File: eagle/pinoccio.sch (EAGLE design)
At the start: 60 parts, among them IC1 ATMEGA16U2QFN32, J1 AVR_SPI_PRG_6, Q1 16MHz, Q2 32.768k, Q3 16MHz, U1 MCP73831, U2 TPS78233, U4 ATMEGA128RFA1, X1 USB-MICROB, Y2 ANTENNA2SMD5

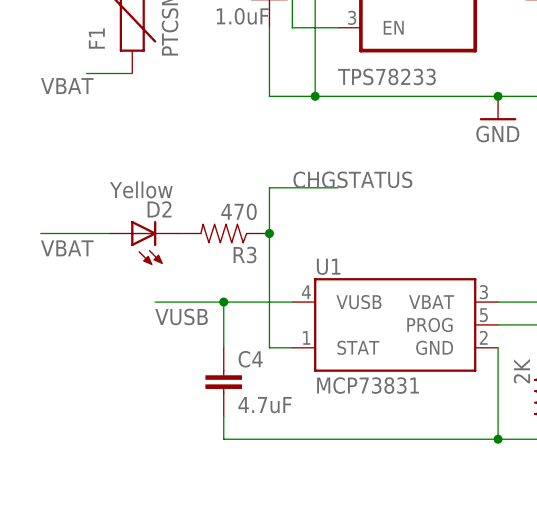
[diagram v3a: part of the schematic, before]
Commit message: Adjust a couple of spacing issues
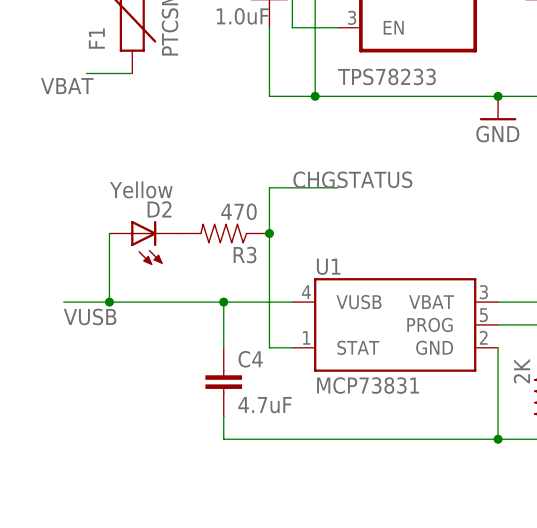
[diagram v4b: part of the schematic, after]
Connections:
- net VBAT: no longer D2.A
- net VUSB: now also D2.A
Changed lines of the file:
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@@
 <segment>
 <wire x1="25.4" y1="17.78" x2="25.4" y2="22.86" width="0.1524" layer="91"/>
-<label x="17.78" y="20.32" size="1.778" layer="95"/>
+<label x="7.62" y="20.32" size="1.778" layer="95"/>
 <pinref part="C4" gate="G$1" pin="1"/>
-<wire x1="25.4" y1="22.86" x2="17.78" y2="22.86" width="0.1524" layer="91"/>
+<wire x1="25.4" y1="22.86" x2="12.7" y2="22.86" width="0.1524" layer="91"/>
 <pinref part="U1" gate="G$1" pin="VUSB"/>
+<wire x1="12.7" y1="22.86" x2="7.62" y2="22.86" width="0.1524" layer="91"/>
 <wire x1="25.4" y1="22.86" x2="33.02" y2="22.86" width="0.1524" layer="91"/>
 <junction x="25.4" y="22.86"/>
+<pinref part="D2" gate="G$1" pin="A"/>
+<wire x1="12.7" y1="30.48" x2="12.7" y2="22.86" width="0.1524" layer="91"/>
+<junction x="12.7" y="22.86"/>
 </segment>
 <segment>
@@
 <label x="137.16" y="12.7" size="1.778" layer="95"/>
 </segment>
-<segment>
-<pinref part="D2" gate="G$1" pin="A"/>
-<wire x1="12.7" y1="30.48" x2="5.08" y2="30.48" width="0.1524" layer="91"/>
-<label x="5.08" y="27.94" size="1.778" layer="95"/>
-</segment>
 </net>

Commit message: Tagging for v0.9
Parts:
- R1: value 10k -> 2k
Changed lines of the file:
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@@
 <grid distance="0.1" unitdist="inch" unit="inch" style="lines" multiple="1" display="no" altdistance="0.01" altunitdist="inch" altunit="inch"/>
 <layers>
-<layer number="1" name="Top" color="4" fill="1" visible="no" active="no"/>
-<layer number="2" name="Route2" color="1" fill="3" visible="no" active="no"/>
-<layer number="3" name="Route3" color="4" fill="3" visible="no" active="no"/>
-<layer number="4" name="Route4" color="1" fill="4" visible="no" active="no"/>
-<layer number="5" name="Route5" color="4" fill="4" visible="no" active="no"/>
-<layer number="6" name="Route6" color="1" fill="8" visible="no" active="no"/>
-<layer number="7" name="Route7" color="4" fill="8" visible="no" active="no"/>
-<layer number="8" name="Route8" color="1" fill="2" visible="no" active="no"/>
-<layer number="9" name="Route9" color="4" fill="2" visible="no" active="no"/>
-<layer number="10" name="Route10" color="1" fill="7" visible="no" active="no"/>
-<layer number="11" name="Route11" color="4" fill="7" visible="no" active="no"/>
-<layer number="12" name="Route12" color="1" fill="5" visible="no" active="no"/>
-<layer number="13" name="Route13" color="4" fill="5" visible="no" active="no"/>
-<layer number="14" name="Route14" color="1" fill="6" visible="no" active="no"/>
-<layer number="15" name="Route15" color="4" fill="6" visible="no" active="no"/>
-<layer number="16" name="Bottom" color="1" fill="1" visible="no" active="no"/>
-<layer number="17" name="Pads" color="2" fill="1" visible="no" active="no"/>
-<layer number="18" name="Vias" color="2" fill="1" visible="no" active="no"/>
-<layer number="19" name="Unrouted" color="6" fill="1" visible="no" active="no"/>
-<layer number="20" name="Dimension" color="6" fill="1" visible="no" active="no"/>
-<layer number="21" name="tPlace" color="16" fill="1" visible="no" active="no"/>
-<layer number="22" name="bPlace" color="14" fill="1" visible="no" active="no"/>
-<layer number="23" name="tOrigins" color="15" fill="1" visible="no" active="no"/>
-<layer number="24" name="bOrigins" color="15" fill="1" visible="no" active="no"/>
-<layer number="25" name="tNames" color="7" fill="1" visible="no" active="no"/>
-<layer number="26" name="bNames" color="7" fill="1" visible="no" active="no"/>
-<layer number="27" name="tValues" color="7" fill="1" visible="no" active="no"/>
-<layer number="28" name="bValues" color="7" fill="1" visible="no" active="no"/>
+<layer number="1" name="Top" color="4" fill="1" visible="yes" active="no"/>
+<layer number="2" name="Route2" color="1" fill="3" visible="yes" active="no"/>
+<layer number="3" name="Route3" color="4" fill="3" visible="yes" active="no"/>
+<layer number="4" name="Route4" color="1" fill="4" visible="yes" active="no"/>
+<layer number="5" name="Route5" color="4" fill="4" visible="yes" active="no"/>
+<layer number="6" name="Route6" color="1" fill="8" visible="yes" active="no"/>
+<layer number="7" name="Route7" color="4" fill="8" visible="yes" active="no"/>
+<layer number="8" name="Route8" color="1" fill="2" visible="yes" active="no"/>
+<layer number="9" name="Route9" color="4" fill="2" visible="yes" active="no"/>
+<layer number="10" name="Route10" color="1" fill="7" visible="yes" active="no"/>
+<layer number="11" name="Route11" color="4" fill="7" visible="yes" active="no"/>
+<layer number="12" name="Route12" color="1" fill="5" visible="yes" active="no"/>
+<layer number="13" name="Route13" color="4" fill="5" visible="yes" active="no"/>
+<layer number="14" name="Route14" color="1" fill="6" visible="yes" active="no"/>
+<layer number="15" name="Route15" color="4" fill="6" visible="yes" active="no"/>
+<layer number="16" name="Bottom" color="1" fill="1" visible="yes" active="no"/>
+<layer number="17" name="Pads" color="2" fill="1" visible="yes" active="no"/>
+<layer number="18" name="Vias" color="2" fill="1" visible="yes" active="no"/>
+<layer number="19" name="Unrouted" color="6" fill="1" visible="yes" active="no"/>
+<layer number="20" name="Dimension" color="6" fill="1" visible="yes" active="no"/>
+<layer number="21" name="tPlace" color="16" fill="1" visible="yes" active="no"/>
+<layer number="22" name="bPlace" color="14" fill="1" visible="yes" active="no"/>
+<layer number="23" name="tOrigins" color="15" fill="1" visible="yes" active="no"/>
+<layer number="24" name="bOrigins" color="15" fill="1" visible="yes" active="no"/>
+<layer number="25" name="tNames" color="7" fill="1" visible="yes" active="no"/>
+<layer number="26" name="bNames" color="7" fill="1" visible="yes" active="no"/>
+<layer number="27" name="tValues" color="7" fill="1" visible="yes" active="no"/>
+<layer number="28" name="bValues" color="7" fill="1" visible="yes" active="no"/>
 <layer number="29" name="tStop" color="5" fill="1" visible="no" active="no"/>
 <layer number="30" name="bStop" color="7" fill="6" visible="no" active="no"/>
@@
 <layer number="35" name="tGlue" color="7" fill="4" visible="no" active="no"/>
 <layer number="36" name="bGlue" color="7" fill="5" visible="no" active="no"/>
-<layer number="37" name="tTest" color="7" fill="1" visible="no" active="no"/>
-<layer number="38" name="bTest" color="7" fill="1" visible="no" active="no"/>
+<layer number="37" name="tTest" color="7" fill="1" visible="yes" active="no"/>
+<layer number="38" name="bTest" color="7" fill="1" visible="yes" active="no"/>
 <layer number="39" name="tKeepout" color="4" fill="11" visible="no" active="no"/>
 <layer number="40" name="bKeepout" color="1" fill="11" visible="no" active="no"/>
@@
 <layer number="44" name="Drills" color="7" fill="1" visible="no" active="no"/>
 <layer number="45" name="Holes" color="7" fill="1" visible="no" active="no"/>
-<layer number="46" name="Milling" color="3" fill="1" visible="no" active="no"/>
-<layer number="47" name="Measures" color="7" fill="1" visible="no" active="no"/>
-<layer number="48" name="Document" color="7" fill="1" visible="no" active="no"/>
-<layer number="49" name="Reference" color="7" fill="1" visible="no" active="no"/>
-<layer number="50" name="dxf" color="7" fill="1" visible="no" active="no"/>
-<layer number="51" name="tDocu" color="6" fill="1" visible="no" active="no"/>
-<layer number="52" name="bDocu" color="7" fill="1" visible="no" active="no"/>
-<layer number="53" name="tGND_GNDA" color="7" fill="9" visible="no" active="no"/>
-<layer number="54" name="bGND_GNDA" color="1" fill="9" visible="no" active="no"/>
-<layer number="56" name="wert" color="7" fill="1" visible="no" active="no"/>
+<layer number="46" name="Milling" color="3" fill="1" visible="yes" active="no"/>
+<layer number="47" name="Measures" color="7" fill="1" visible="yes" active="no"/>
+<layer number="48" name="Document" color="7" fill="1" visible="yes" active="no"/>
+<layer number="49" name="Reference" color="7" fill="1" visible="yes" active="no"/>
+<layer number="50" name="dxf" color="7" fill="1" visible="yes" active="no"/>
+<layer number="51" name="tDocu" color="6" fill="1" visible="yes" active="no"/>
+<layer number="52" name="bDocu" color="7" fill="1" visible="yes" active="no"/>
+<layer number="53" name="tGND_GNDA" color="7" fill="9" visible="yes" active="no"/>
+<layer number="54" name="bGND_GNDA" color="1" fill="9" visible="yes" active="no"/>
+<layer number="56" name="wert" color="7" fill="1" visible="yes" active="no"/>
 <layer number="91" name="Nets" color="2" fill="1" visible="yes" active="yes"/>
 <layer number="92" name="Busses" color="1" fill="1" visible="yes" active="yes"/>
@@
 <part name="U$3" library="Pinoccio" deviceset="SWITCH-DUAL-MOSFET" device="SOT23-8"/>
 <part name="GND7" library="SparkFun" deviceset="GND" device=""/>
-<part name="R1" library="Pinoccio" deviceset="RESISTOR" device="0402-RES" value="10k"/>
+<part name="R1" library="Pinoccio" deviceset="RESISTOR" device="0402-RES" value="2k"/>
 <part name="GND6" library="SparkFun" deviceset="GND" device=""/>
 <part name="GND8" library="SparkFun" deviceset="GND" device=""/>

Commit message: v0.10 update
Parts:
- removed D3: DIODE-SCHOTTKY0402, Pinoccio:DIODE-SCHOTTKY0402
- removed R5: 10k, Pinoccio:RESISTOR0402-RES
- removed R7: 40k, Pinoccio:RESISTOR0402-RES
- added C1: 100nF, Pinoccio:CAP0402-CAP
- added Q4: MOSFET-PCHANNELSMD, Pinoccio:MOSFET-PCHANNELSMD
- added R16, R19: 100k, Pinoccio:RESISTOR0402-RES
- added R20: 10k, Pinoccio:RESISTOR0402-RES
- added R21, R23: DNI, Pinoccio:RESISTOR0402-RES
- added R22, R24: 0, Pinoccio:RESISTOR0402-RES
- added R6: 470, Pinoccio:RESISTOR0402-RES
- added U$2: SWITCH-MOSFETTDFN4, Pinoccio:SWITCH-MOSFETTDFN4
- added U$4: MAX17048DFN8, Pinoccio:MAX17048DFN8
- JP3, JP5: value FIDUCIALUFIDUCIAL -> FIDUCIAL1X2; device Pinoccio:FIDUCIALUFIDUCIAL -> Pinoccio:FIDUCIAL1X2
- R4: value 2K -> 3K
- U1: value MCP73831 -> MCP73832; device Pinoccio:MCP73831 -> Pinoccio:MCP73832
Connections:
- removed net BATTCHECK: U$3.P3-ON2, U4.PD6
- removed net D0: JP-L.10, U4.~PB7
- removed net D1: JP-L.11, U4.~PE3
- removed net N$11: R4.1, U1.PROG
- removed net N$14: D3.A, R5.1, R7.2
- removed net N$3: R5.2, U$3.P5-VOUT2
- removed net N$8: F1.2, JP1.1, S2.S
- new net BATTALRT: U$4.~ALRT, U4.PG5~
- new net BKPK-BUS: JP-L.2, U4.PD6
- new net D7: JP-L.15, U4.*PE6
- new net D8: JP-L.16, U4.*PE7
- new net N$27: R22.2, R23.1, R24.1
- new net N$28: R24.2, Y2.SIGNAL
- new net N$51: JP1.1, Q4.S, S2.S, U$2.OUT
- new net PROG: IC1.PD4(INT5/AIN3), R4.1, U1.PROG
- new net RESET-EN: JP-L.3, R6.1
- new net SHIELDBAT-EN: R16.1, U$3.P3-ON2, U4.PD5
- new net UCAP: C18.1, IC1.AVCC, IC1.UCAP, IC1.VCC, J1.2
- new net VBAT-AS: C6.1, JP1.2, S2.P, U$3.P4-VIN2, U2.EN, U2.IN
- net A7: no longer D3.C
- net AREF: now also C1.1
- net D2: now also JP-L.10, U4.~PB7; no longer JP-L.12, U4.~*PE4
- net D3: now also JP-L.11, U4.~PE3; no longer JP-L.13, U4.~*PE5
- net D4: now also JP-L.12, U4.~*PE4; no longer JP-L.14, U4.PE2
- net D5: now also JP-L.13, U4.~*PE5; no longer JP-L.15, U4.*PE6
- net D6: now also JP-L.14, U4.PE2; no longer JP-L.16, U4.*PE7
- net GND: now also C1.2, R16.2, R19.2, R20.2, R21.2, R23.2, U$2.GND, U$4.CTG, U$4.GND, U$4.QSTRT; no longer JP-L.2, R7.1, U4.AVSS@PADDLE
- net N$12: now also F1.2, Q4.D; no longer C18.1, IC1.AVCC, IC1.UCAP, IC1.VCC
- net N$4: now also R21.1, R22.1; no longer Y2.SIGNAL
- net RESET: now also R6.2; no longer JP-L.3
- net SCL: now also U$4.SCL
- net SDA: now also U$4.SDA
- net SHIELDVCC-EN: now also R19.1, U4.PD4; no longer U4.PD5
- net VBAT: now also U$4.CELL, U$4.VDD
- net VBAT-AE: now also U$3.P5-VOUT2; no longer C6.1, JP1.2, S2.P, U$3.P4-VIN2, U2.EN, U2.IN
- net VCC: no longer J1.2, R1.1
- net VUSB: now also Q4.G, R1.1, R20.1, U$2.IN, U$2.ON
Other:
- note added: "0.10"
- note removed: "0.9"
- moved on the sheet: C11, C19, C2, C4, C5, C6, C7, C8, C9, D1, F1, JP1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

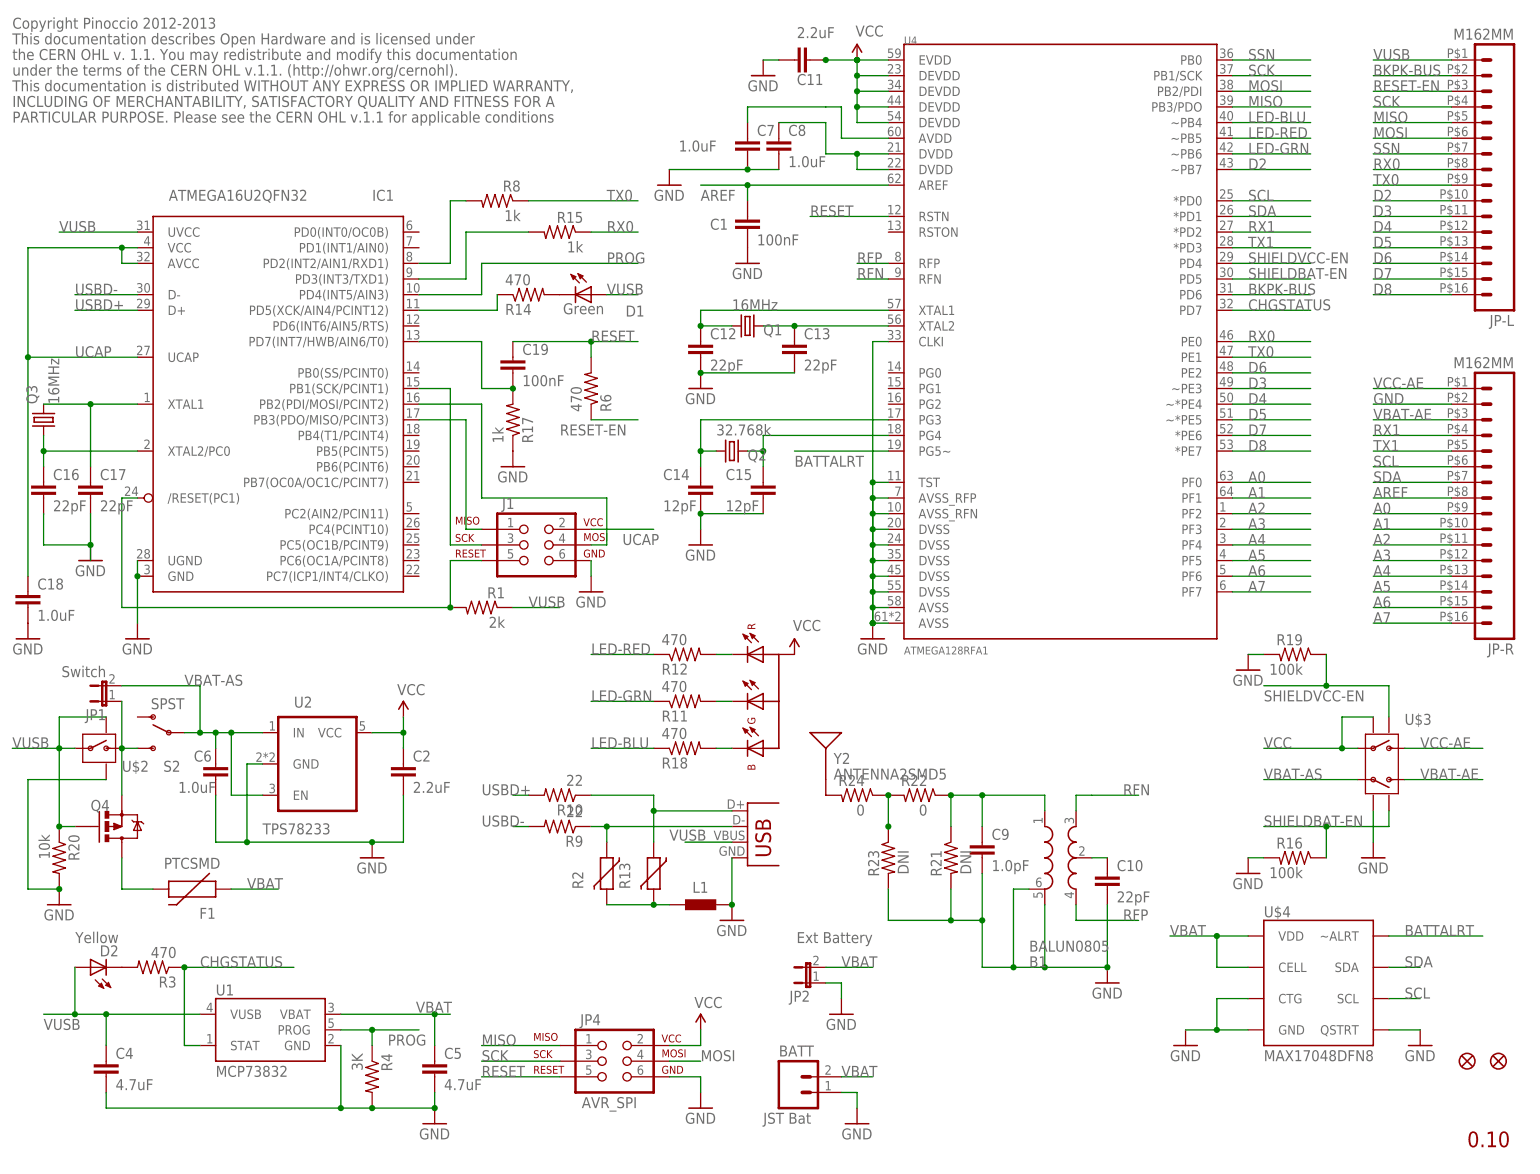
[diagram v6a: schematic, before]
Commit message: Add addl contributors, and swap dual load switch for single load switch
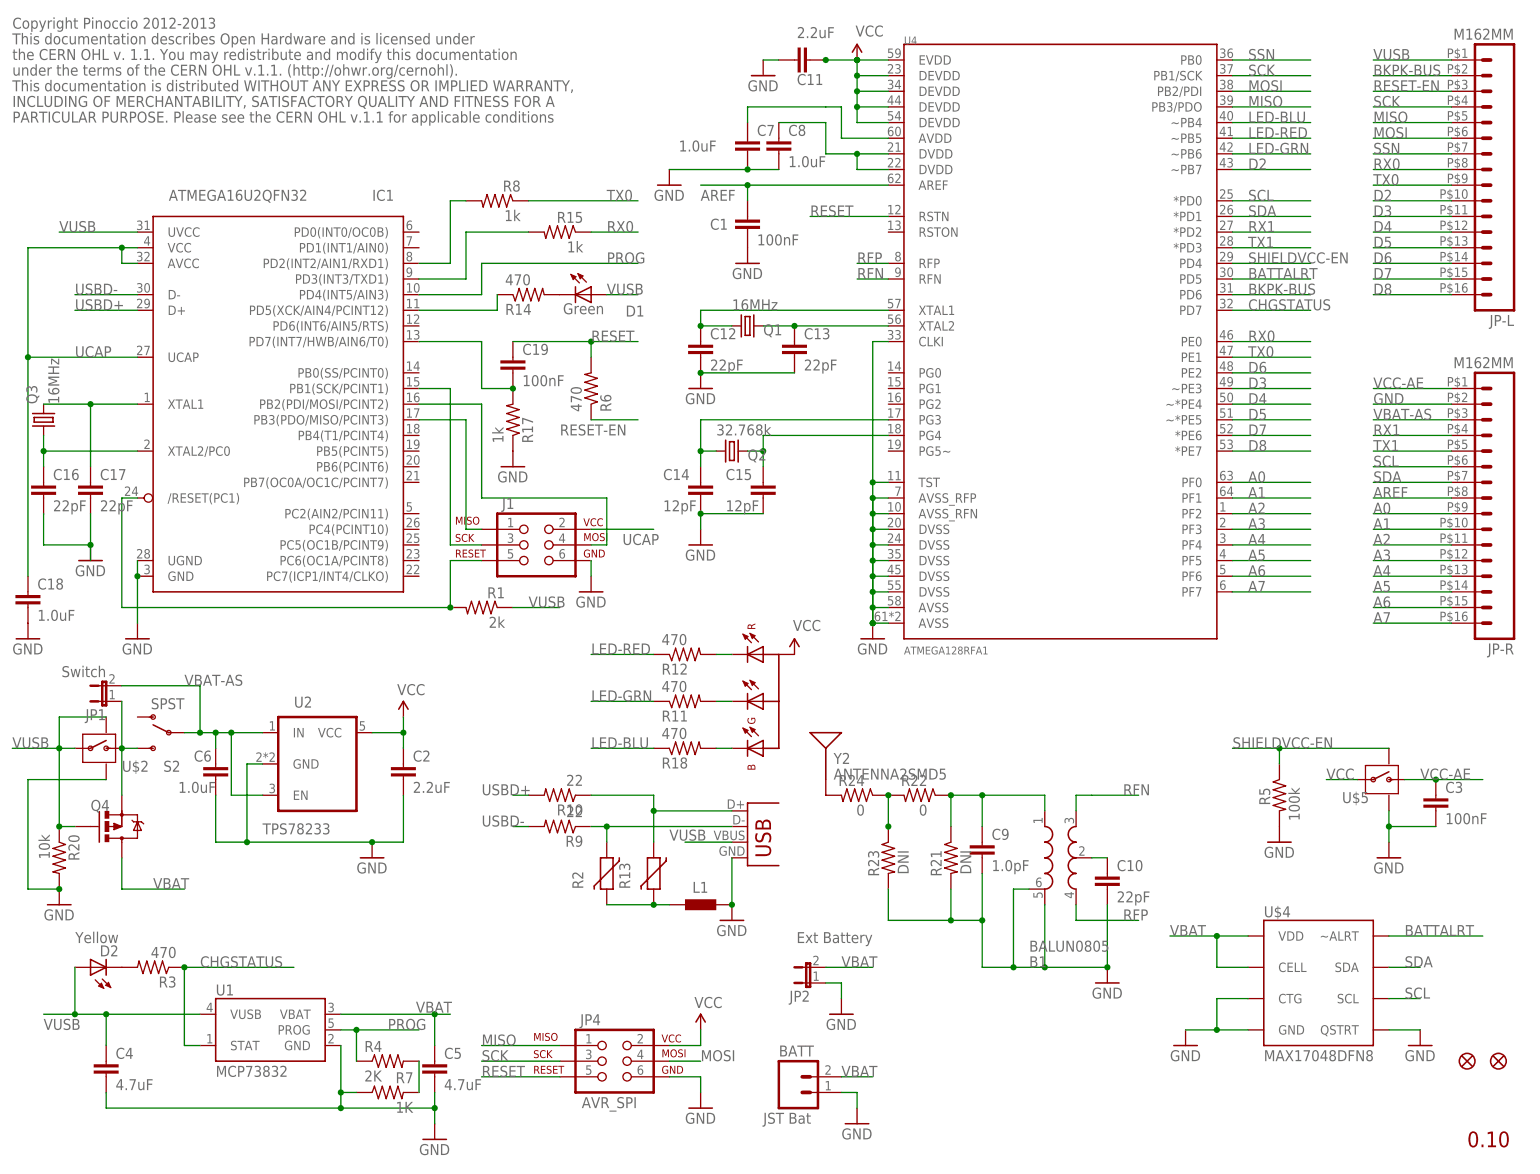
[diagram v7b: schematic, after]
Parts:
- removed F1: PTCSMD, SparkFun:PTCSMD
- removed R16, R19: 100k, Pinoccio:RESISTOR0402-RES
- removed U$3: SWITCH-DUAL-MOSFETSOT23-8, Pinoccio:SWITCH-DUAL-MOSFETSOT23-8
- added C3: 100nF, Pinoccio:CAP0402-CAP
- added R5: 100k, Pinoccio:RESISTOR0402-RES
- added R7: 1K, Pinoccio:RESISTOR0402-RES
- added U$5: SWITCH-MOSFETTDFN4, Pinoccio:SWITCH-MOSFETTDFN4
- R4: value 3K -> 2K
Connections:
- removed net N$12: F1.2, Q4.D
- removed net SHIELDBAT-EN: R16.1, U$3.P3-ON2, U4.PD5
- removed net VBAT-AE: JP-R.3, U$3.P5-VOUT2
- new net N$8: R4.2, R7.2
- net BATTALRT: now also U4.PD5; no longer U4.PG5~
- net GND: now also C3.2, R5.2, R7.1, U$5.GND; no longer R16.2, R19.2, R4.2, U$3.P6-GND
- net SHIELDVCC-EN: now also R5.1, U$5.ON; no longer R19.1, U$3.P2-ON1
- net VBAT: now also Q4.D; no longer F1.1
- net VBAT-AS: now also JP-R.3; no longer U$3.P4-VIN2
- net VCC: now also U$5.IN; no longer U$3.P7-SR, U$3.VIN1
- net VCC-AE: now also C3.1, U$5.OUT; no longer U$3.P8-VOUT1
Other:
- moved on the sheet: R4
